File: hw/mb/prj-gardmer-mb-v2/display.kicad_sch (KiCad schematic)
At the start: 23 parts, among them Q5 BC807, Q6 BC807, Q7 BC807, Q8 BC807, U7 KW4-804AVB, U8 74HC595

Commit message: Assigned footprints to schematic symbols.
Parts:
- C19, R32, R33, R34, R35, R36, R37, R38, R39, R40, R41, R42, R43, R44, R45, R46, R47: footprint (none) -> alf64:Generic_0805
- Q5, Q6, Q7, Q8: footprint (none) -> alf64:SOT-23-3
- U7: footprint (none) -> alf64:KW4-804AVB
- U8: footprint (none) -> alf64:SO-16_3.9x9.9mm_P1.27mm
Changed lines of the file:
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@@
 			)
 		)
-		(property "Footprint" ""
+		(property "Footprint" "alf64:Generic_0805"
 			(at 121.158 130.81 90)
 			(effects
@@
 			)
 		)
-		(property "Footprint" ""
+		(property "Footprint" "alf64:SOT-23-3"
 			(at 133.35 73.66 0)
 			(effects
@@
 			)
 		)
-		(property "Footprint" ""
+		(property "Footprint" "alf64:Generic_0805"
 			(at 41.6052 34.29 0)
 			(effects
@@
 			)
 		)
-		(property "Footprint" ""
+		(property "Footprint" "alf64:Generic_0805"
 			(at 104.902 40.64 90)
 			(effects
@@
 			)
 		)
-		(property "Footprint" ""
+		(property "Footprint" "alf64:Generic_0805"
 			(at 126.238 130.81 90)
 			(effects
@@
 			)
 		)
-		(property "Footprint" ""
+		(property "Footprint" "alf64:Generic_0805"
 			(at 136.398 130.81 90)
 			(effects
@@
 			)
 		)
-		(property "Footprint" ""
+		(property "Footprint" "alf64:Generic_0805"
 			(at 131.318 130.81 90)
 			(effects
@@
 			)
 		)
-		(property "Footprint" ""
+		(property "Footprint" "alf64:Generic_0805"
 			(at 141.478 130.81 90)
 			(effects
@@
 			)
 		)
-		(property "Footprint" ""
+		(property "Footprint" "alf64:SOT-23-3"
 			(at 162.56 73.66 0)
 			(effects
@@
 			)
 		)
-		(property "Footprint" ""
+		(property "Footprint" "alf64:Generic_0805"
 			(at 156.718 130.81 90)
 			(effects
@@
 			)
 		)
-		(property "Footprint" ""
+		(property "Footprint" "alf64:Generic_0805"
 			(at 97.79 70.358 90)
 			(effects
@@
 			)
 		)
-		(property "Footprint" ""
+		(property "Footprint" "alf64:Generic_0805"
 			(at 151.638 130.81 90)
 			(effects
@@
 			)
 		)
-		(property "Footprint" ""
+		(property "Footprint" "alf64:Generic_0805"
 			(at 97.79 57.658 90)
 			(effects
@@
 			)
 		)
-		(property "Footprint" ""
+		(property "Footprint" "alf64:Generic_0805"
 			(at 120.142 40.64 90)
 			(effects
@@
 			)
 		)
-		(property "Footprint" ""
+		(property "Footprint" "alf64:Generic_0805"
 			(at 135.382 40.64 90)
 			(effects
@@
 			)
 		)
-		(property "Footprint" ""
+		(property "Footprint" "alf64:SOT-23-3"
 			(at 148.59 73.66 0)
 			(effects
@@
 			)
 		)
-		(property "Footprint" ""
+		(property "Footprint" "alf64:SOT-23-3"
 			(at 118.11 73.66 0)
 			(effects
@@
 			)
 		)
-		(property "Footprint" ""
+		(property "Footprint" "alf64:Generic_0805"
 			(at 146.558 130.81 90)
 			(effects
@@
 			)
 		)
-		(property "Footprint" ""
+		(property "Footprint" "alf64:KW4-804AVB"
 			(at 134.62 121.92 0)
 			(effects
@@
 			)
 		)
-		(property "Footprint" ""
+		(property "Footprint" "alf64:SO-16_3.9x9.9mm_P1.27mm"
 			(at 82.55 148.59 0)
 			(effects
@@
 			)
 		)
-		(property "Footprint" ""
+		(property "Footprint" "alf64:Generic_0805"
 			(at 97.79 64.008 90)
 			(effects
@@
 			)
 		)
-		(property "Footprint" ""
+		(property "Footprint" "alf64:Generic_0805"
 			(at 149.352 40.64 90)
 			(effects
@@
 			)
 		)
-		(property "Footprint" ""
+		(property "Footprint" "alf64:Generic_0805"
 			(at 97.79 51.308 90)
 			(effects

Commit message: Updated schematic (footprints assign), PCB and footprints: - Changed the 'Generic' footprints that were used for capacitors, resistors and fuses into specific ones (I.e. Generic_0805 is replaced by C_0805 and R_0805). - Differentiated the D_0805 and LED_0805 footprints
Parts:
- C19: footprint alf64:Generic_0805 -> alf64:C_0805
- R32, R33, R34, R35, R36, R37, R38, R39, R40, R41, R42, R43, R44, R45, R46, R47: footprint alf64:Generic_0805 -> alf64:R_0805
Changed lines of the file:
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@@
 			)
 		)
-		(property "Footprint" "alf64:Generic_0805"
+		(property "Footprint" "alf64:R_0805"
 			(at 121.158 130.81 90)
 			(effects
@@
 			)
 		)
-		(property "Footprint" "alf64:Generic_0805"
+		(property "Footprint" "alf64:C_0805"
 			(at 41.6052 34.29 0)
 			(effects
@@
 			)
 		)
-		(property "Footprint" "alf64:Generic_0805"
+		(property "Footprint" "alf64:R_0805"
 			(at 104.902 40.64 90)
 			(effects
@@
 			)
 		)
-		(property "Footprint" "alf64:Generic_0805"
+		(property "Footprint" "alf64:R_0805"
 			(at 126.238 130.81 90)
 			(effects
@@
 			)
 		)
-		(property "Footprint" "alf64:Generic_0805"
+		(property "Footprint" "alf64:R_0805"
 			(at 136.398 130.81 90)
 			(effects
@@
 			)
 		)
-		(property "Footprint" "alf64:Generic_0805"
+		(property "Footprint" "alf64:R_0805"
 			(at 131.318 130.81 90)
 			(effects
@@
 			)
 		)
-		(property "Footprint" "alf64:Generic_0805"
+		(property "Footprint" "alf64:R_0805"
 			(at 141.478 130.81 90)
 			(effects
@@
 			)
 		)
-		(property "Footprint" "alf64:Generic_0805"
+		(property "Footprint" "alf64:R_0805"
 			(at 156.718 130.81 90)
 			(effects
@@
 			)
 		)
-		(property "Footprint" "alf64:Generic_0805"
+		(property "Footprint" "alf64:R_0805"
 			(at 97.79 70.358 90)
 			(effects
@@
 			)
 		)
-		(property "Footprint" "alf64:Generic_0805"
+		(property "Footprint" "alf64:R_0805"
 			(at 151.638 130.81 90)
 			(effects
@@
 			)
 		)
-		(property "Footprint" "alf64:Generic_0805"
+		(property "Footprint" "alf64:R_0805"
 			(at 97.79 57.658 90)
 			(effects
@@
 			)
 		)
-		(property "Footprint" "alf64:Generic_0805"
+		(property "Footprint" "alf64:R_0805"
 			(at 120.142 40.64 90)
 			(effects
@@
 			)
 		)
-		(property "Footprint" "alf64:Generic_0805"
+		(property "Footprint" "alf64:R_0805"
 			(at 135.382 40.64 90)
 			(effects
@@
 			)
 		)
-		(property "Footprint" "alf64:Generic_0805"
+		(property "Footprint" "alf64:R_0805"
 			(at 146.558 130.81 90)
 			(effects
@@
 			)
 		)
-		(property "Footprint" "alf64:Generic_0805"
+		(property "Footprint" "alf64:R_0805"
 			(at 97.79 64.008 90)
 			(effects
@@
 			)
 		)
-		(property "Footprint" "alf64:Generic_0805"
+		(property "Footprint" "alf64:R_0805"
 			(at 149.352 40.64 90)
 			(effects
@@
 			)
 		)
-		(property "Footprint" "alf64:Generic_0805"
+		(property "Footprint" "alf64:R_0805"
 			(at 97.79 51.308 90)
 			(effects

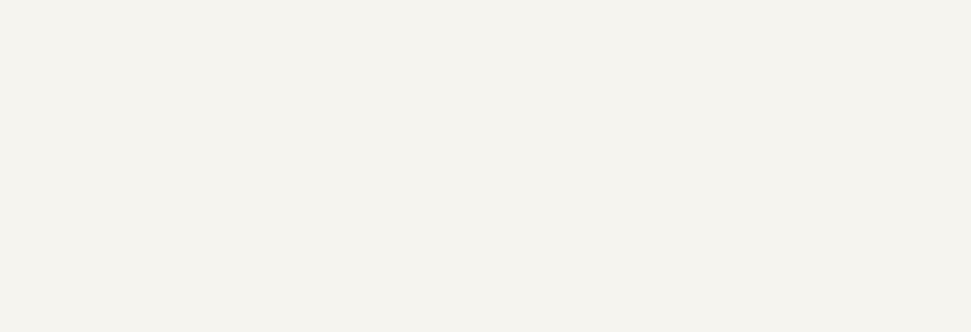
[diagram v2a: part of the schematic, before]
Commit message: Updated the hw release of prj-gardmer-mb-v2 rev001: - reorganized files in catalogues - added schematic in .pdf - added top & bottom elements on pcb in .pdf - added bom
Updated schematic:
- added a title, rev and date to the drawing info table on each sheet
- excluded test points ('TP' elements) from BOM

Updated PCB:
- added a title, rev and date to the drawing info table
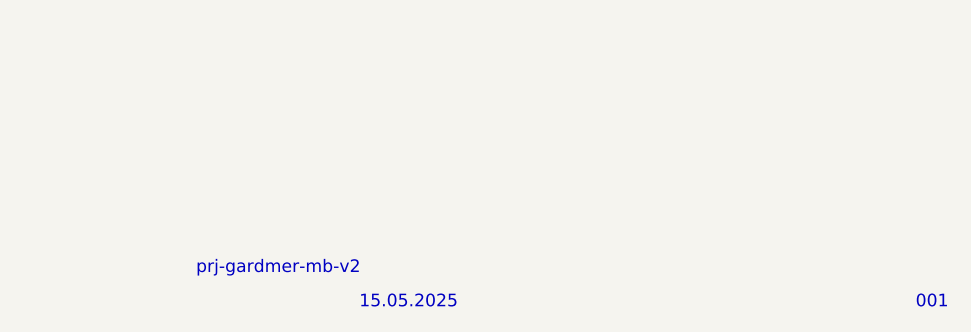
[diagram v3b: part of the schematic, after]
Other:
- note added: "001"
- note added: "15.05.2025"
- note added: "prj-gardmer-mb-v2"
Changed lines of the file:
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@@
+		)
+	)
+	(text "001"
+		(exclude_from_sim no)
+		(at 271.78 193.294 0)
+		(effects
+			(font
+				(size 1.397 1.397)
+			)
+		)
+	)
+	(text "prj-gardmer-mb-v2"
+		(exclude_from_sim no)
+		(at 199.136 189.484 0)
+		(effects
+			(font
+				(size 1.397 1.397)
+			)
+		)
+	)
+	(text "15.05.2025"
+		(exclude_from_sim no)
+		(at 213.614 193.294 0)
+		(effects
+			(font
+				(size 1.397 1.397)
+			)
 		)
 	)
